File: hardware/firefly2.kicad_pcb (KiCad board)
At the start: 2 copper layers, 41.5 x 41.5 mm, 18 parts, among them J1 10118194-0001LF, P2 CONN_01X03, P3 CONN_01X04, P4 CONN_01X05, P5 CONN_01X01, U1 SAM_D11C, U2 RFM69CW, U3 MIC5504

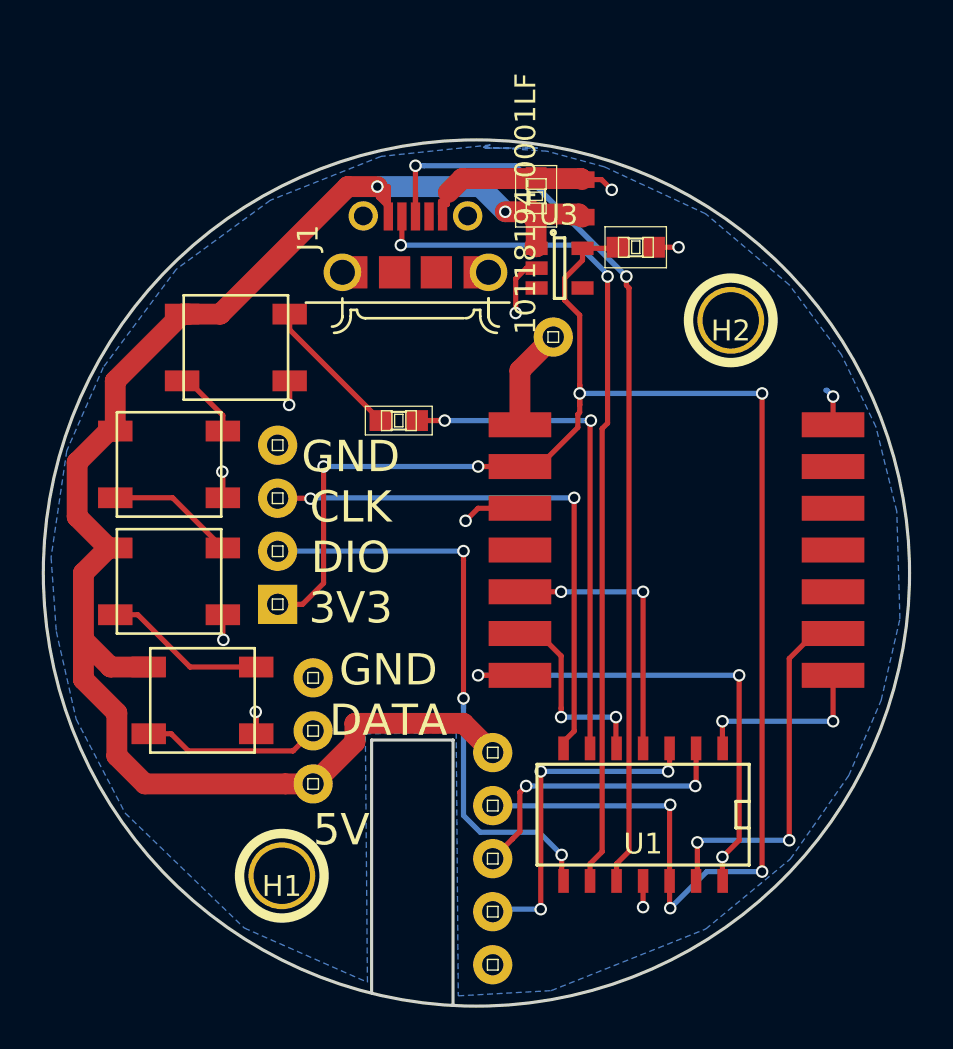
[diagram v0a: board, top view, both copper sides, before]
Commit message: Hardware v2.1 Mark orientation for LEDs and radio. Tie enable high on the LDO. Add vertical USB connector and fix horizontal USB connector.
Change-Id: I3b6b9a9fcd473732bc67a64c80cbd03d1b6050b8
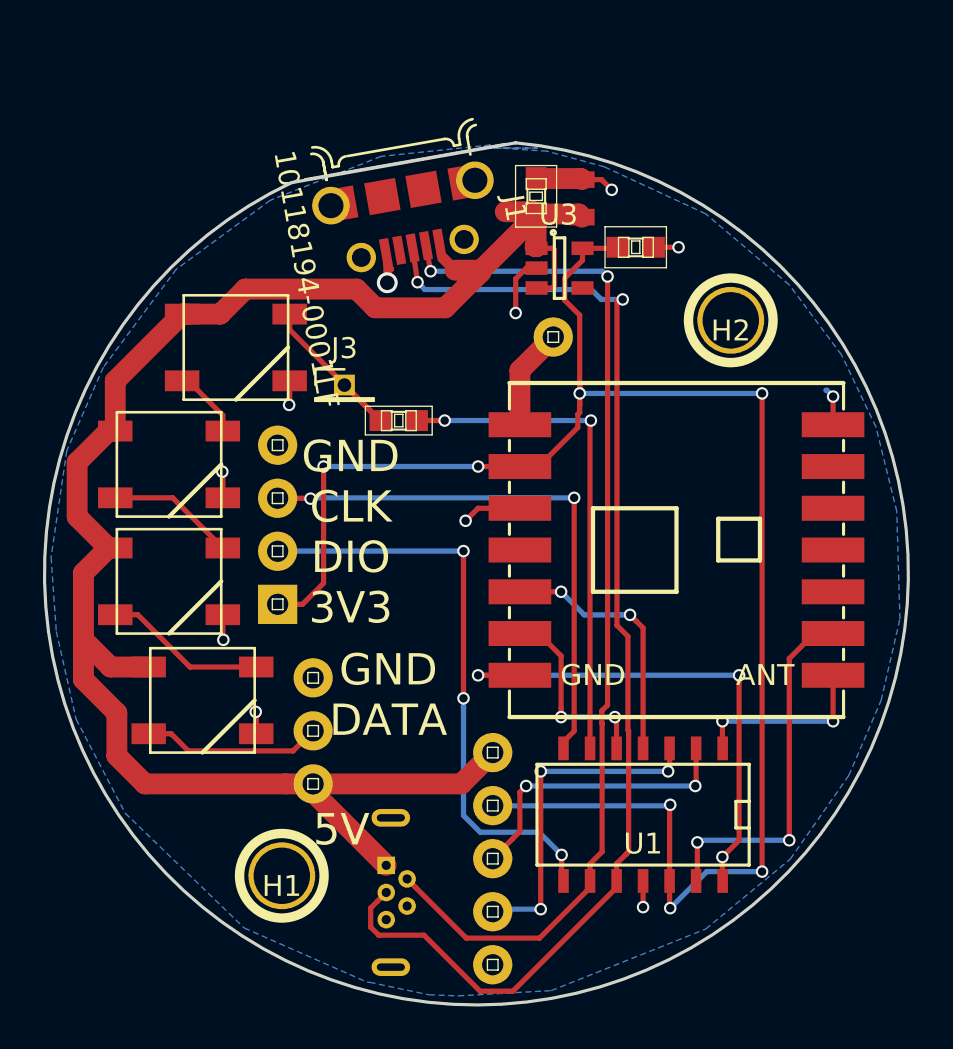
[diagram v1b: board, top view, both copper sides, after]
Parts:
- added J2: 614105150721, Connector_USB:USB_Micro-B_Wuerth-614105150721_Vertical, B.Cu at (155.7, 77.5)
- added J3: CONN_01X01, Pin_Headers:Pin_Header_Straight_1x01_Pitch1.27mm, F.Cu at (153.7, 54.5)
- D1, D2, D3, D4: footprint SparkFun-LED:WS2812B -> homebrew:WS2812B
- U2: footprint SparkFun-RF:RFM69CW-XXXS2 -> homebrew:RFM69CW-XXXS2
- moved J1 3.85 mm to (156.5, 45.3), turned to 190 degrees
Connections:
- U3 pad 3: Net-(U3-Pad3) -> +5V
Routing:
- net +5V: track 77.9 -> 88.4 mm, vias 2 -> 0
- net USB_D-: track 41.3 -> 50.4 mm
- net USB_D+: track 50.0 -> 57.9 mm
- net Net-(D1-Pad4): track 6.93 -> 9.38 mm
- net RADIO_MOSI: track 13.4 -> 12.4 mm
- net GND: track 26.5 -> 25.6 mm, vias 10 -> 11
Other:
- board size 41.5 x 41.5 mm -> 41.4 x 41.3 mm
- board text added: "Firefly V2.1"
- board text removed: "Firefly V2.0"

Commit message: Place v2.1 parts (no routing yet)
Change-Id: I3c64d8efe2df87153508bcfdb10d42841a7add0c
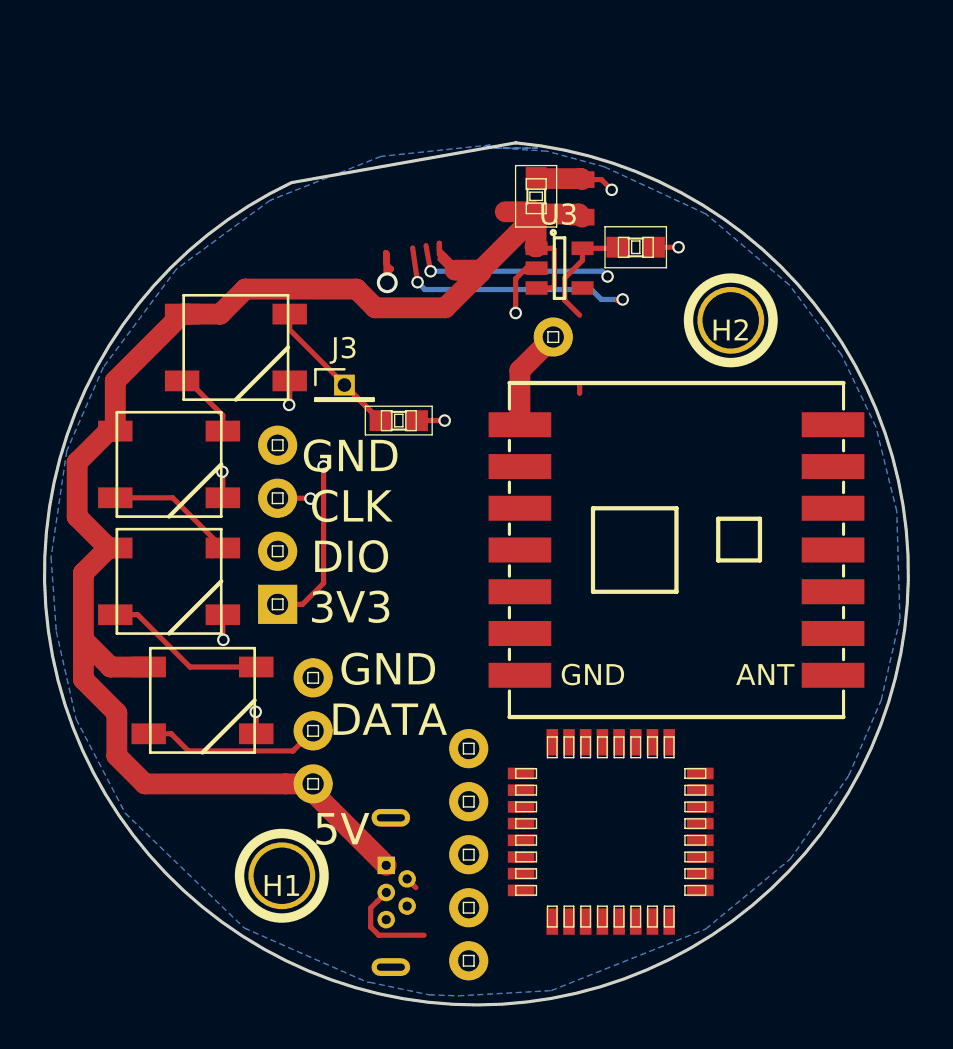
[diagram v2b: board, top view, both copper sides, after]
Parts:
- removed J1: 10118194-0001LF, 10118194-0001LF:FRAMATOME_10118194-0001LF
- U1: value SAM_D11C -> SAMD21E18; footprint SMD_Packages:SOIC-14_N -> SparkFun-DigitalIC:TQFP32-08
- moved U1 1.70 mm to (166.4, 75.9), turned to 0 degrees
- moved P4 1.17 mm to (159.7, 71.9)
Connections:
- D1 pad 4: Net-(D1-Pad4) -> LED_INTERNAL
- J3 pad 1: Net-(D1-Pad4) -> LED_INTERNAL
- P3 pad 1: +3V3 -> +5V
- U1 pad 1: RADIO_MISO -> AUX1
- U1 pad 10: USB_D+ -> GND
- U1 pad 11: GND -> RADIO_MOSI
- U1 pad 12: +3V3 -> RADIO_SCK
- U1 pad 13: RADIO_DIO0 -> RADIO_MISO
- U1 pad 2: AUX1 -> AUX2
- U1 pad 3: AUX2 -> Net-(U1-Pad3)
- U1 pad 4: RADIO_MOSI -> Net-(U1-Pad4)
- U1 pad 5: RADIO_SCK -> Net-(U1-Pad5)
- U1 pad 6: LED_INTERNAL -> Net-(U1-Pad6)
- U1 pad 7: ARM_SWCLK -> Net-(U1-Pad7)
- U1 pad 8: ARM_SWDIO -> LED_INTERNAL
- U1 pad 9: USB_D- -> +3V3
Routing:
- net +3V3: track 84.6 -> 7.78 mm, vias 7 -> 0
- net USB_D+: track 57.9 -> 16.8 mm
- net USB_D-: track 50.4 -> 10.4 mm
- net ARM_SWDIO: track 28.6 -> 0.01 mm, vias 3 -> 0
- net ARM_SWCLK: track 26.4 -> 1.64 mm, vias 2 -> 1
- net RADIO_NSS: track 24.7 -> 0.00 mm, vias 3 -> 0
- net LED_INTERNAL: track 24.1 -> 4.50 mm, vias 2 -> 1
- net RADIO_DIO0: track 17.6 -> 0.90 mm, vias 2 -> 0
- net AUX2: track 16.2 -> 0.00 mm, vias 3 -> 0
- net AUX1: track 14.1 -> 0.00 mm, vias 2 -> 0
- net RADIO_MOSI: track 12.4 -> 0.00 mm, vias 2 -> 0
- net GND: track 25.6 -> 14.0 mm, vias 11 -> 7
- net RADIO_MISO: track 8.80 -> 0.00 mm, vias 2 -> 0
- net RADIO_SCK: track 9.45 -> 0.90 mm, vias 2 -> 0
- net (no net): track 0.00 -> 5.31 mm, vias 0 -> 1
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
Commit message: Route v2.1 rev of board
Change-Id: Ib0707158455f74b9999820dd41ec12748fe4f6ba
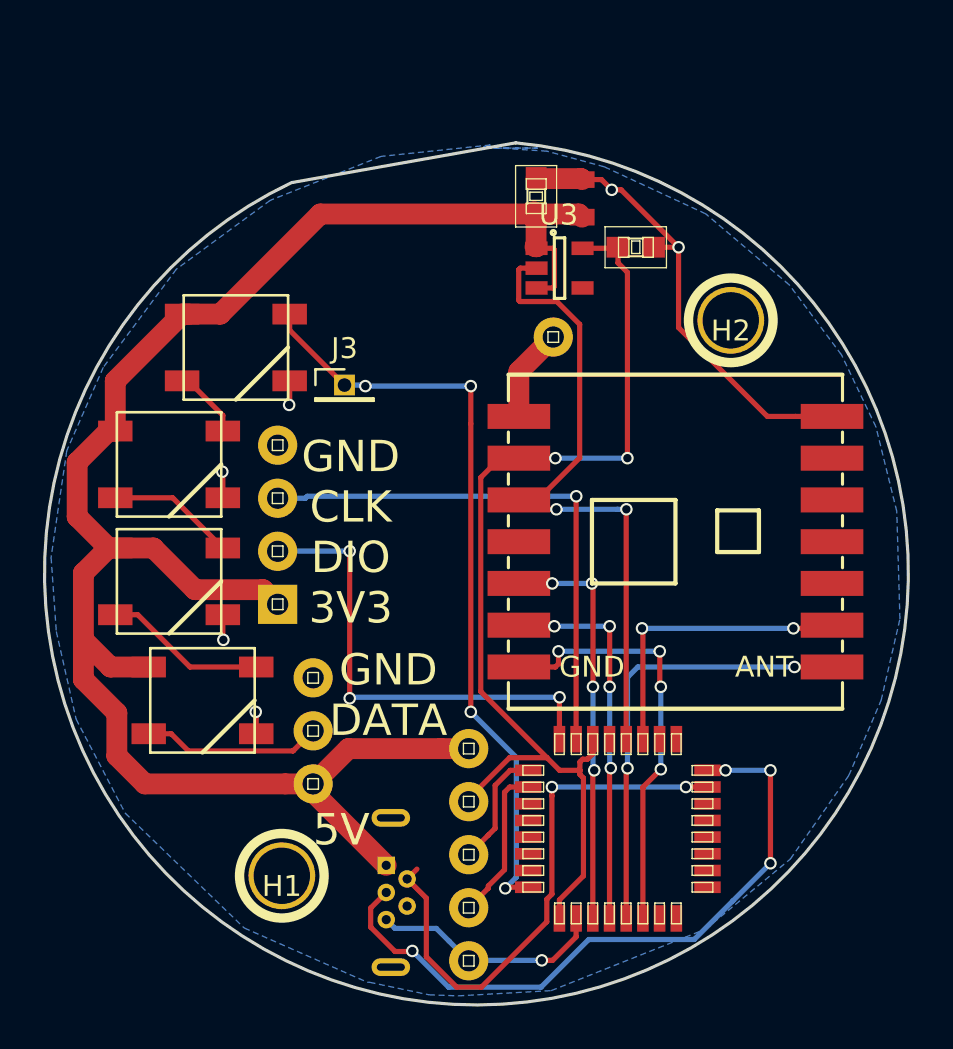
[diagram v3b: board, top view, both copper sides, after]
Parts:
- removed R1: 220, SparkFun-Resistors:0603
- moved U2 0.40 mm to (169.6, 62.0)
- moved U1 0.37 mm to (166.8, 75.7)
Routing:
- net GND: track 14.0 -> 73.5 mm, vias 7 -> 9
- net +3V3: track 7.78 -> 52.0 mm, vias 0 -> 2
- net LED_INTERNAL: track 4.50 -> 36.9 mm, vias 1 -> 4
- net ARM_SWCLK: track 1.64 -> 26.0 mm
- net ARM_SWDIO: track 0.01 -> 22.6 mm, vias 0 -> 3
- net RADIO_MISO: track 0.00 -> 21.6 mm, vias 0 -> 2
- net RADIO_NSS: track 0.00 -> 20.6 mm, vias 0 -> 4
- net RADIO_MOSI: track 0.00 -> 19.6 mm, vias 0 -> 4
- net RADIO_SCK: track 0.90 -> 19.3 mm, vias 0 -> 4
- net USB_D-: track 10.4 -> 26.4 mm
- net USB_D+: track 16.8 -> 32.2 mm, vias 2 -> 4
- net RADIO_DIO0: track 0.90 -> 15.4 mm, vias 0 -> 2
- net AUX2: track 0.00 -> 7.48 mm
- net Net-(D1-Pad4): track 6.23 -> 0.00 mm
- net AUX1: track 0.00 -> 5.73 mm
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
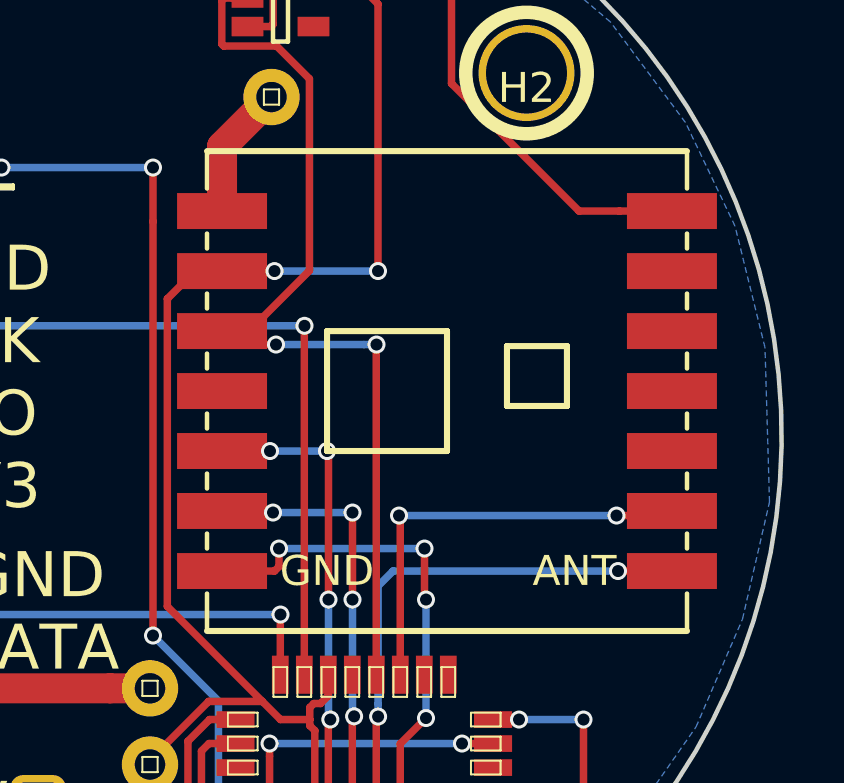
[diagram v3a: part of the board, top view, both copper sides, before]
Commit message: Fix radio silkscreen orientation for v2.1
Change-Id: I934a96829cceb58ae09e96efa49570f37a8bb193
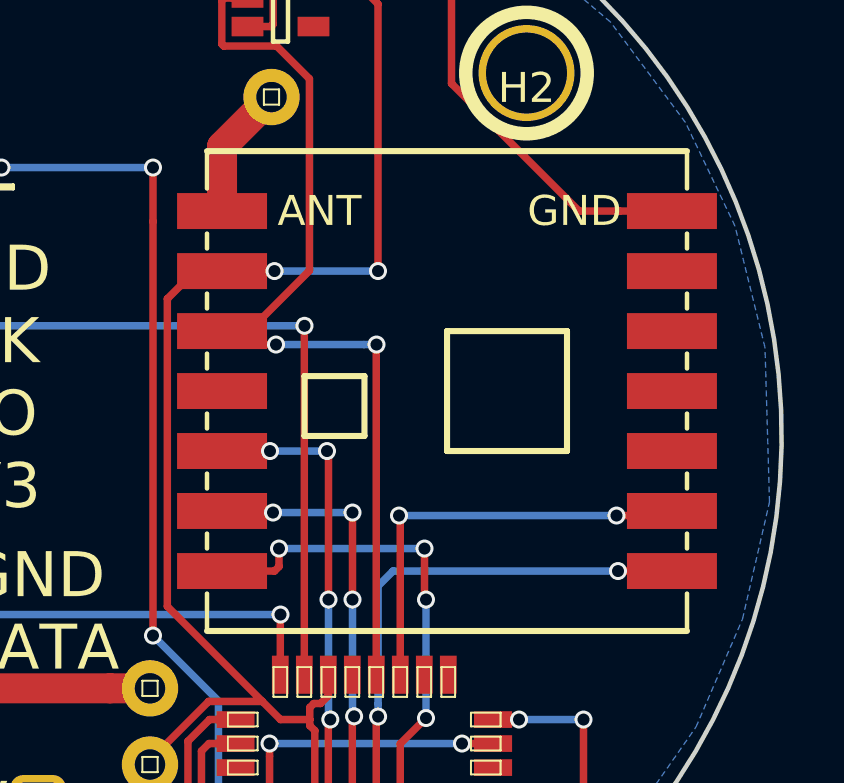
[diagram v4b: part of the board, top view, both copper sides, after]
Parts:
- U2: footprint homebrew:RFM69CW-XXXS2 -> homebrew:RFM69CW
